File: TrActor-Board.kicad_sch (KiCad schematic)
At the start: 0 parts

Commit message: add gitignore
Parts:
- added U1: nRF52833_QDxx, Package_DFN_QFN:QFN-40-1EP_5x5mm_P0.4mm_EP3.6x3.6mm, symbol MCU_Nordic:nRF52833_QDxx
- added U2: DW3210, TrActor:QFN-40-1EP_5x5mm_P0.4mm, symbol TrActor:DW3210
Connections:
- new net: U1.18 (VDD), U1.30 (VDD), U1.40 (VDD), U1.8 (VDD)
- new net: U1.37 (VSS), U1.41 (VSS)
- new net RF_GND: U2.10 (RF_GND), U2.11 (RF_GND), U2.12 (RF_GND), U2.14 (RF_GND), U2.15 (RF_GND), U2.16 (RF_GND), U2.17 (RF_GND), U2.19 (RF_GND), U2.20 (RF_GND)
- new net VSS: U2.39 (VSS), U2.40 (VSS)

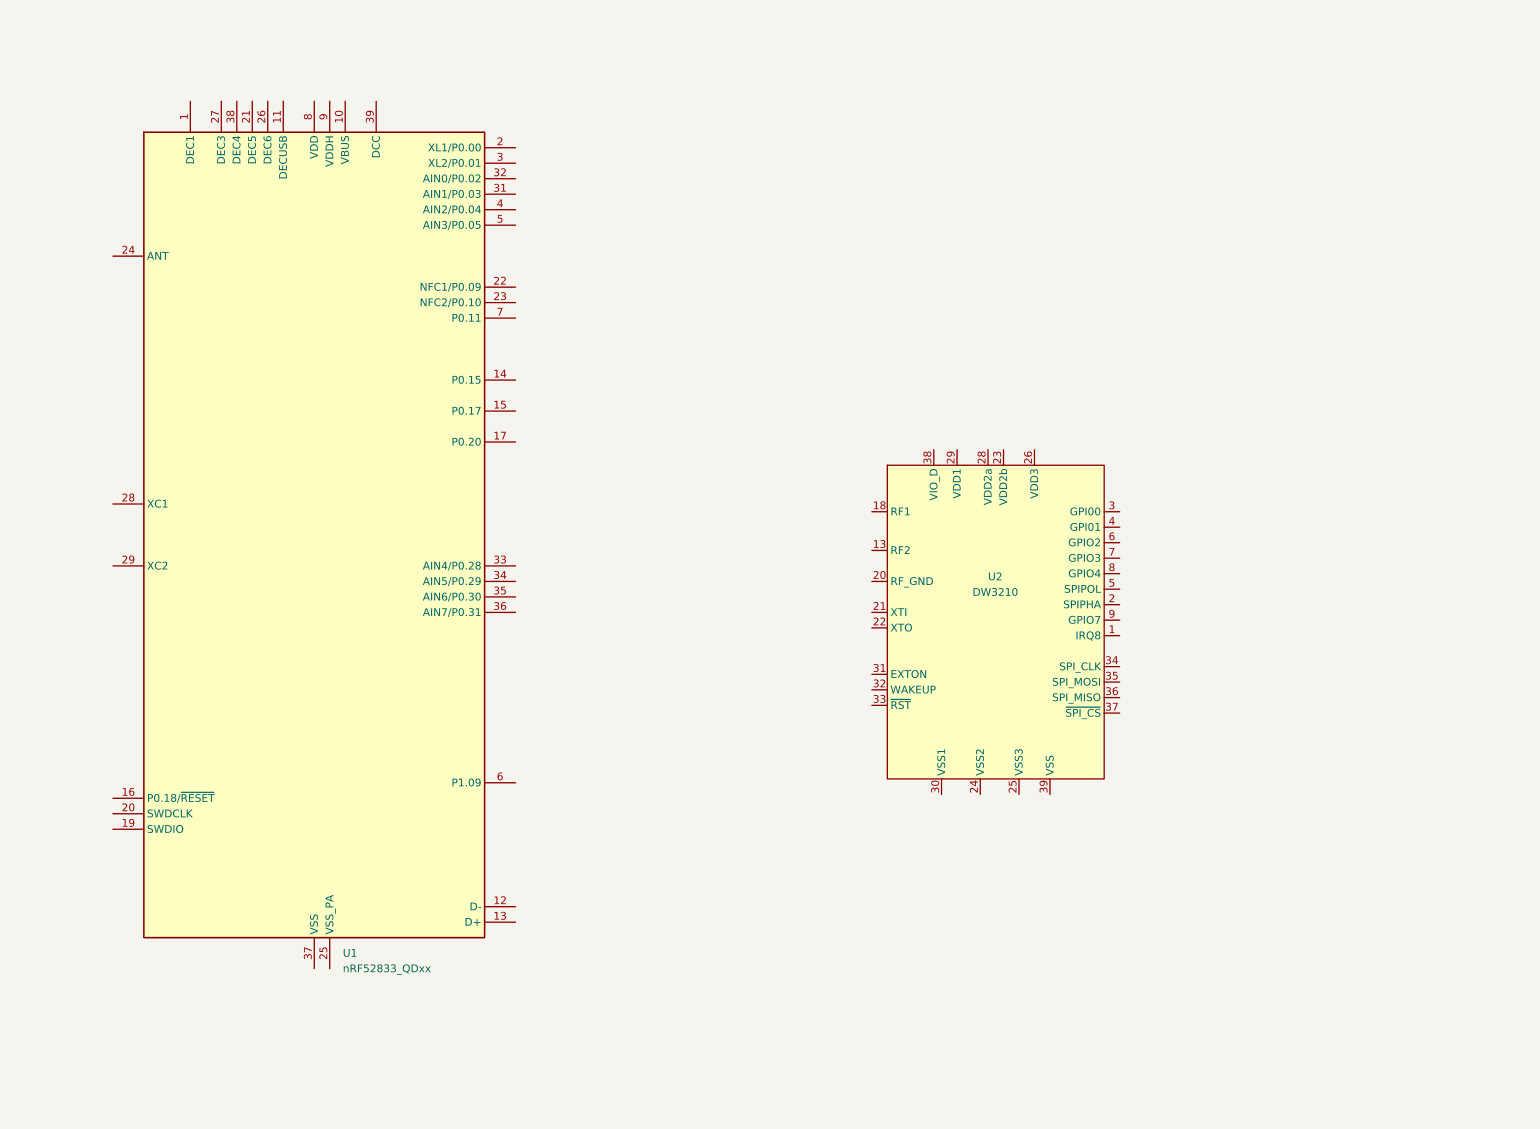
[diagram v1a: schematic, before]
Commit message: first step of schematic capture
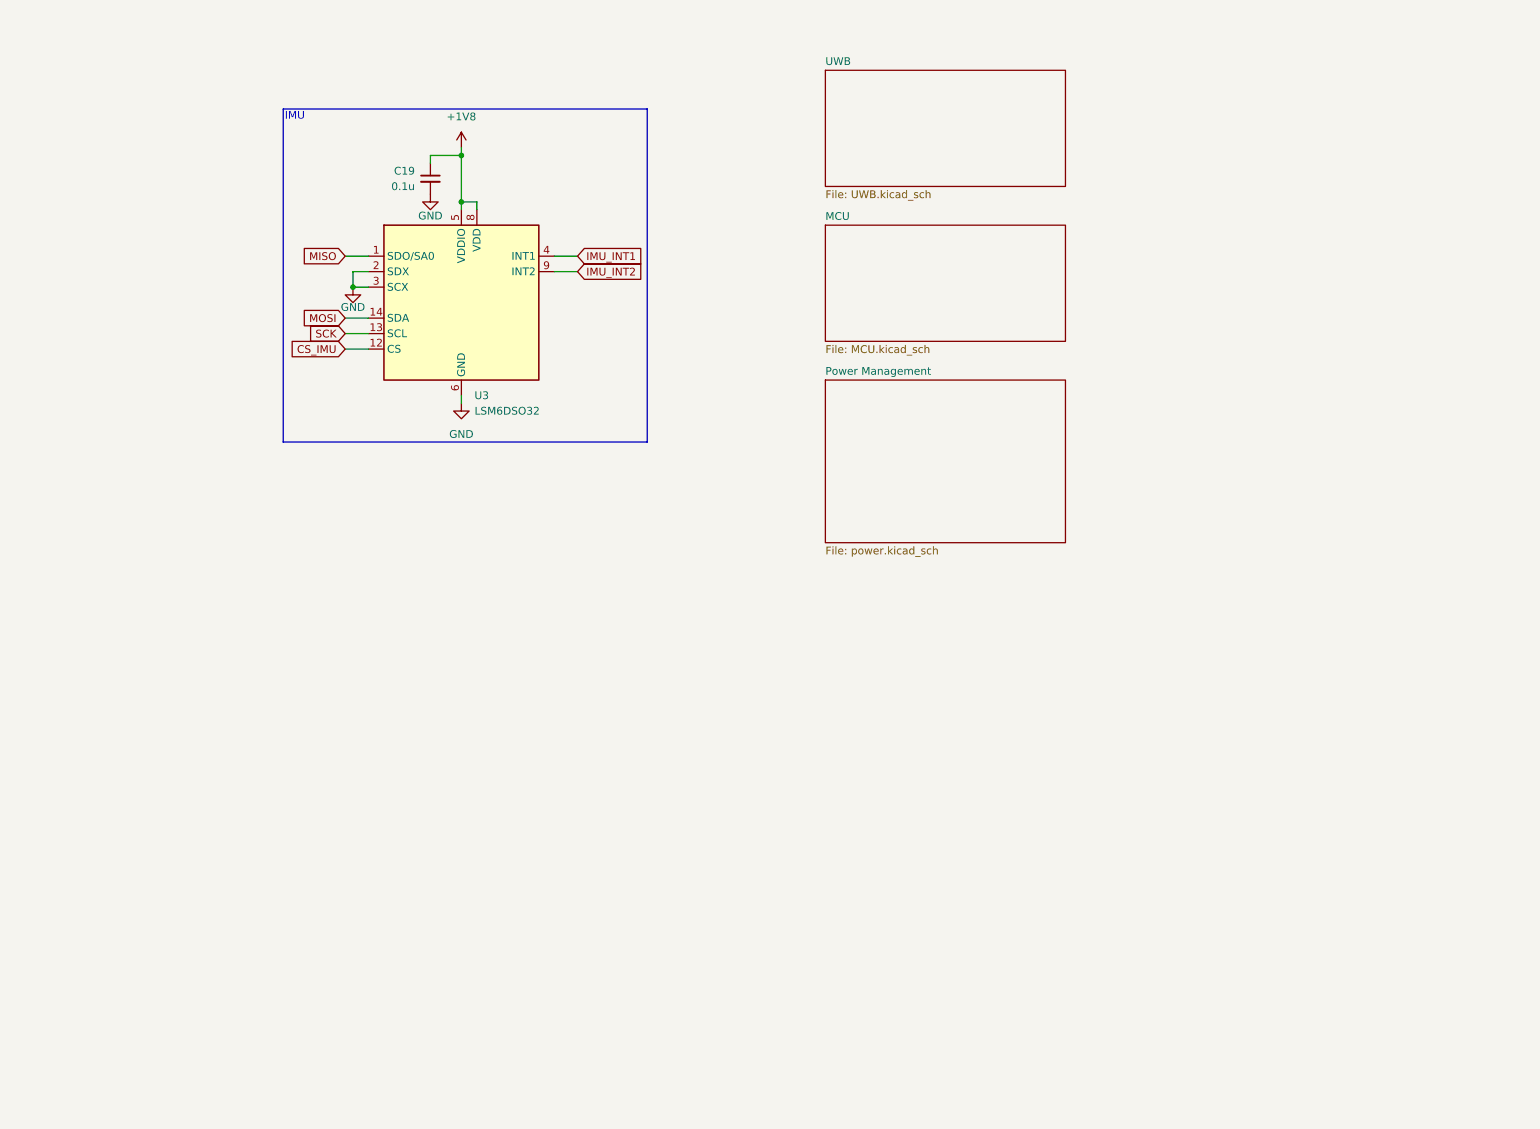
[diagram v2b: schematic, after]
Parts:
- removed U1: nRF52833_QDxx, Package_DFN_QFN:QFN-40-1EP_5x5mm_P0.4mm_EP3.6x3.6mm, symbol MCU_Nordic:nRF52833_QDxx
- removed U2: DW3210, TrActor:QFN-40-1EP_5x5mm_P0.4mm, symbol TrActor:DW3210
- added C19: 0.1u, symbol Device:C_Small
- added U3: LSM6DSO32, Package_LGA:LGA-14_3x2.5mm_P0.5mm_LayoutBorder3x4y, symbol Sensor_Motion:LSM6DS3
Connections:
- new net +1V8: C19.1, U3.5 (VDDIO), U3.8 (VDD)
- new net CS_IMU: U3.12 (CS)
- new net GND: C19.2, U3.2 (SDX), U3.3 (SCX), U3.6 (GND), U3.7 (GND)
- new net IMU_INT1: U3.4 (INT1)
- new net IMU_INT2: U3.9 (INT2)
- new net MISO: U3.1 (SDO/SA0)
- new net MOSI: U3.14 (SDA)
- new net SCK: U3.13 (SCL)
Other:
- added sheet MCU (MCU.kicad_sch)
- added sheet Power Management (power.kicad_sch)
- added sheet UWB (UWB.kicad_sch)
- note added: "IMU"

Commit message: schematic capture like half done, need to do a lot of the smaller things
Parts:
- added F1: 500mA 6V, Fuse:Fuse_0603_1608Metric, symbol Device:Polyfuse_Small
- added J3: GCT4720, TrActor:GCT_USB4720-03-A_REVA, symbol Connector:USB_C_Receptacle_USB2.0_16P
- added R11, R12: 0, symbol Device:R_Small_US
- added U6: USBLC6-2P6, Package_TO_SOT_SMD:SOT-666, symbol Power_Protection:USBLC6-2P6
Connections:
- net GND: now also J3.A1 (GND), J3.A12 (GND), J3.B1 (GND), J3.B12 (GND), U6.2 (GND)
- new net: F1.1, J3.A4 (VBUS), J3.A9 (VBUS), J3.B4 (VBUS), J3.B9 (VBUS), U6.5 (VBUS)
- new net: J3.A6 (D+), J3.B6 (D+), U6.3 (I/O2)
- new net: J3.A7 (D-), J3.B7 (D-), U6.1 (I/O1)
- new net: R11.2, U6.4 (I/O2)
- new net: R12.1, U6.6 (I/O1)
- new net USB+: R11.1
- new net USB-: R12.2
- new net USB_CC1: J3.A5 (CC1)
- new net USB_CC2: J3.B5 (CC2)
- new net VUSB: F1.2
- no-connect marks 0 -> 3
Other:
- note added: "TO:DO: - USB D+/- series resistor selection (check nRF datasheet) - battery cell connector - battery NTC connector - power button - reset button (or jumper?)"
- note added: "USB Connector"
- moved on the sheet: C19, U3

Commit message: all schematic done but RF
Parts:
- added C14: 4.7n, Capacitor_SMD:C_0402_1005Metric, symbol Device:C_Small
- added F2: 500mA 6V, Fuse:Fuse_0603_1608Metric, symbol Device:Polyfuse_Small
- added J4: Battery, symbol Connector_Generic_MountingPin:Conn_01x04_MountingPin
- added JP1: Reset, symbol Jumper:Jumper_2_Open
- added R13: 1M, Resistor_SMD:R_0402_1005Metric, symbol Device:R_Small_US
- added SW1: Power, symbol Switch:SW_Push
- added SW2: Reset, symbol Switch:SW_Push
- added TP10: BTN_POWER, symbol Connector:TestPoint
- added TP11: BTN_RESET, symbol Connector:TestPoint
- added TP12: GND, symbol Connector:TestPoint_Alt
- added TP13: D-, symbol Connector:TestPoint
- added TP14: D+, symbol Connector:TestPoint
- added TP22: IMU_INT1, symbol Connector:TestPoint
- added TP23: IMU_INT2, symbol Connector:TestPoint
- added TP5: VUSB, symbol Connector:TestPoint_Alt
- added TP9: BATT, symbol Connector:TestPoint_Alt
- C19: footprint (none) -> Capacitor_SMD:C_0402_1005Metric
- R11, R12: value 0 -> 0R; footprint (none) -> Resistor_SMD:R_0402_1005Metric
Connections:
- net GND: now also C14.2, J4.1 (Pin_1), J4.3 (Pin_3), JP1.1 (A), R13.2, SW1.1, SW2.1, TP12.1
- net IMU_INT1: now also TP22.1
- net IMU_INT2: now also TP23.1
- net at F1.1, J3.A4 (VBUS), J3.A9 (VBUS)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: now also TP5.1
- net at J3.A6 (D+), J3.B6 (D+), U6.3 (I/O2): now also TP14.1
- net at J3.A7 (D-), J3.B7 (D-), U6.1 (I/O1): now also TP13.1
- net at J3.SH (SHIELD): now also C14.1, R13.1
- new net: F2.1, J4.4 (Pin_4), TP9.1
- new net +BATT: F2.2
- new net BTN_POWER: SW1.2, TP10.1
- new net BTN_RESET: JP1.2 (B), SW2.2, TP11.1
- new net NTC: J4.2 (Pin_2)
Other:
- note added: "Battery Connector"
- note added: "Buttons"
- note added: "TO:DO: - power button footprint selection - reset button/jumper footprint selection - Battery connector footprint selection - TP Footprint Selection"
- note added: "Taken from DK Schematic"
- note removed: "TO:DO: - USB D+/- series resistor selection (check nRF datasheet) - battery cell connector - battery NTC connector - power button - reset button (or jumper?)"
- moved on the sheet: F1

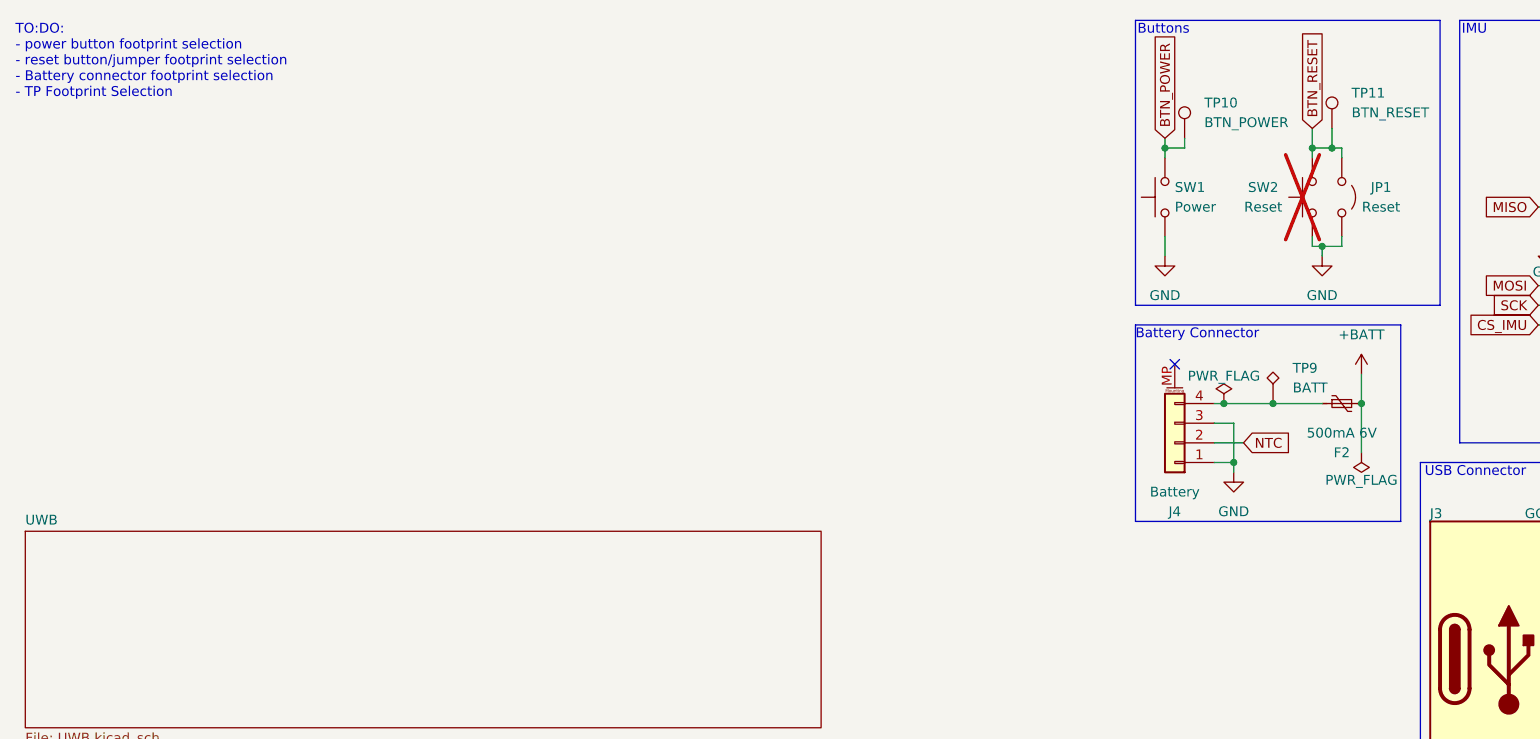
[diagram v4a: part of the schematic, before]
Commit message: schematic & bom done except for UWB RF
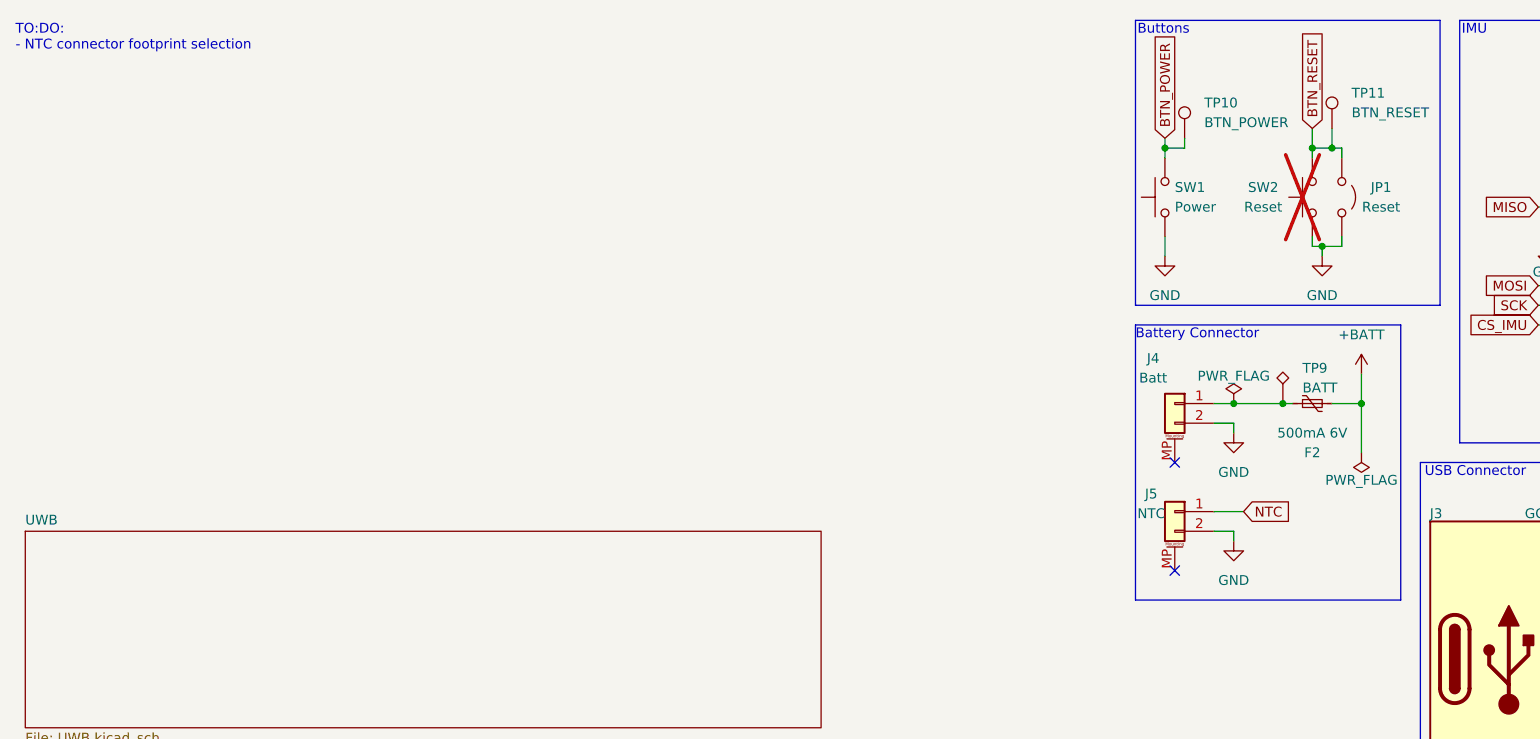
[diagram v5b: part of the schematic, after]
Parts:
- removed J4: Battery, symbol Connector_Generic_MountingPin:Conn_01x04_MountingPin
- added J4: Batt, Connector_JST:JST_PH_S2B-PH-SM4-TB_1x02-1MP_P2.00mm_Horizontal, symbol Connector_Generic_MountingPin:Conn_01x02_MountingPin
- added J5: NTC, symbol Connector_Generic_MountingPin:Conn_01x02_MountingPin
- SW1, SW2: footprint (none) -> Button_Switch_SMD:SW_SPST_EVQP7A
- TP10, TP11, TP13, TP14, TP22, TP23: footprint (none) -> TestPoint:TestPoint_Pad_D1.5mm
- TP12, TP5, TP9: footprint (none) -> TestPoint:TestPoint_Pad_1.5x1.5mm
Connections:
- net GND: now also J4.2 (Pin_2), J5.2 (Pin_2)
- net NTC: now also J5.1 (Pin_1)
- net at F2.1, TP9.1: now also J4.1 (Pin_1)
- no-connect marks 3 -> 4
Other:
- note added: "TO:DO: - NTC connector footprint selection"
- note removed: "TO:DO: - power button footprint selection - reset button/jumper footprint selection - Battery connector footprint selection - TP Footprint Selection"
- moved on the sheet: F2, TP9

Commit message: routing started
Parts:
- J5: footprint (none) -> Connector_JST:JST_SH_SM02B-SRSS-TB_1x02-1MP_P1.00mm_Horizontal
- JP1: footprint (none) -> Connector_PinHeader_2.54mm:PinHeader_1x02_P2.54mm_Vertical_SMD_Pin1Left
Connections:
- net V_PRE: now reaches F1.1, J3.A4 (VBUS), J3.A9 (VBUS), J3.B4 (VBUS), J3.B9 (VBUS), TP5.1, U6.5 (VBUS)
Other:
- moved on the sheet: F1
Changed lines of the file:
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@@
 	)
 	(junction
-		(at 252.73 82.55)
+		(at 259.08 82.55)
 		(diameter 0)
 		(color 0 0 0 0)
@@
 	)
 	(junction
+		(at 241.3 82.55)
+		(diameter 0)
+		(color 0 0 0 0)
+	)
+	(junction
 		(at 181.61 64.77)
 		(diameter 0)
@@
 	)
 	(junction
-		(at 241.3 82.55)
-		(diameter 0)
-		(color 0 0 0 0)
-	)
-	(junction
 		(at 191.77 64.77)
 		(diameter 0)
@@
 	(wire
 		(pts
-			(xy 252.73 82.55) (xy 248.92 82.55)
+			(xy 259.08 82.55) (xy 255.27 82.55)
 		)
 		(stroke
@@
 	(wire
 		(pts
-			(xy 243.84 82.55) (xy 241.3 82.55)
-		)
-		(stroke
-			(width 0)
-			(type default)
-		)
-	)
-	(wire
-		(pts
 			(xy 185.42 33.02) (xy 185.42 31.75)
 		)
@@
 	(wire
 		(pts
+			(xy 241.3 82.55) (xy 250.19 82.55)
+		)
+		(stroke
+			(width 0)
+			(type default)
+		)
+	)
+	(wire
+		(pts
 			(xy 172.72 78.74) (xy 176.53 78.74)
 		)
@@
 	(wire
 		(pts
-			(xy 252.73 80.01) (xy 252.73 82.55)
+			(xy 259.08 80.01) (xy 259.08 82.55)
 		)
 		(stroke
@@
 		)
 	)
+	(global_label "V_PRE"
+		(shape input)
+		(at 243.84 82.55 90)
+		(fields_autoplaced yes)
+		(effects
+			(font
+				(size 1.27 1.27)
+			)
+			(justify left)
+		)
+		(property "Intersheetrefs" "${INTERSHEET_REFS}"
+			(at 243.84 74.4738 90)
+			(hide yes)
+			(show_name no)
+			(do_not_autoplace no)
+			(effects
+				(font
+					(size 1.27 1.27)
+				)
+				(justify left)
+			)
+		)
+	)
 	(global_label "IMU_INT2"
 		(shape input)
@@
 	(symbol
 		(lib_id "power:VBUS")
-		(at 252.73 80.01 0)
+		(at 259.08 80.01 0)
 		(unit 1)
 		(body_style 1)
@@
 		(fields_autoplaced yes)
 		(property "Reference" "#PWR060"
-			(at 252.73 83.82 0)
+			(at 259.08 83.82 0)
 			(hide yes)
 			(show_name no)
@@
 		)
 		(property "Value" "VUSB"
-			(at 252.73 74.93 0)
+			(at 259.08 74.93 0)
 			(show_name no)
 			(do_not_autoplace no)
@@
 		)
 		(property "Footprint" ""
-			(at 252.73 80.01 0)
+			(at 259.08 80.01 0)
 			(hide yes)
 			(show_name no)
@@
 		)
 		(property "Datasheet" ""
-			(at 252.73 80.01 0)
+			(at 259.08 80.01 0)
 			(hide yes)
 			(show_name no)
@@
 		)
 		(property "Description" "Power symbol creates a global label with name \"VBUS\""
-			(at 252.73 80.01 0)
+			(at 259.08 80.01 0)
 			(hide yes)
 			(show_name no)
@@
 			)
 		)
-		(property "Footprint" ""
+		(property "Footprint" "Connector_JST:JST_SH_SM02B-SRSS-TB_1x02-1MP_P1.00mm_Horizontal"
 			(at 167.64 78.74 0)
 			(hide yes)
@@
 	(symbol
 		(lib_id "Device:Polyfuse_Small")
-		(at 246.38 82.55 90)
+		(at 252.73 82.55 90)
 		(unit 1)
 		(body_style 1)
@@
 		(fields_autoplaced yes)
 		(property "Reference" "F1"
-			(at 246.38 76.2 90)
+			(at 252.73 76.2 90)
 			(show_name no)
 			(do_not_autoplace no)
@@
 		)
 		(property "Value" "500mA 6V"
-			(at 246.38 78.74 90)
+			(at 252.73 78.74 90)
 			(show_name no)
 			(do_not_autoplace no)
@@
 		)
 		(property "Footprint" "Fuse:Fuse_0603_1608Metric"
-			(at 251.46 81.28 0)
+			(at 257.81 81.28 0)
 			(hide yes)
 			(show_name no)
@@
 		)
 		(property "Datasheet" ""
-			(at 246.38 82.55 0)
+			(at 252.73 82.55 0)
 			(hide yes)
 			(show_name no)
@@
 		)
 		(property "Description" "Resettable fuse, polymeric positive temperature coefficient, small symbol"
-			(at 246.38 82.55 0)
+			(at 252.73 82.55 0)
 			(hide yes)
 			(show_name no)
@@
 			)
 		)
-		(property "Footprint" ""
+		(property "Footprint" "Connector_PinHeader_2.54mm:PinHeader_1x02_P2.54mm_Vertical_SMD_Pin1Left"
 			(at 189.23 38.1 0)
 			(hide yes)
@@
 	(symbol
 		(lib_id "power:PWR_FLAG")
-		(at 252.73 82.55 0)
+		(at 259.08 82.55 0)
 		(mirror x)
 		(unit 1)
@@
 		(dnp no)
 		(property "Reference" "#FLG02"
-			(at 252.73 84.455 0)
+			(at 259.08 84.455 0)
 			(hide yes)
 			(show_name no)
@@
 		)
 		(property "Value" "PWR_FLAG"
-			(at 252.73 86.106 0)
+			(at 259.08 86.106 0)
 			(show_name no)
 			(do_not_autoplace no)
@@
 		)
 		(property "Footprint" ""
-			(at 252.73 82.55 0)
+			(at 259.08 82.55 0)
 			(hide yes)
 			(show_name no)
@@
 		)
 		(property "Datasheet" ""
-			(at 252.73 82.55 0)
+			(at 259.08 82.55 0)
 			(hide yes)
 			(show_name no)
@@
 		)
 		(property "Description" "Special symbol for telling ERC where power comes from"
-			(at 252.73 82.55 0)
+			(at 259.08 82.55 0)
 			(hide yes)
 			(show_name no)
